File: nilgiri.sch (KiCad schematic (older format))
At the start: 32 parts, among them SW1 SW_PUSH, SW10 SW_PUSH, SW11 SW_PUSH, SW12 SW_PUSH, SW13 SW_PUSH, SW2 SW_PUSH, SW3 SW_PUSH, SW4 SW_PUSH, SW5 SW_PUSH, SW6 SW_PUSH, SW7 SW_PUSH, SW8 SW_PUSH, SW9 SW_PUSH, U1 ProMicro

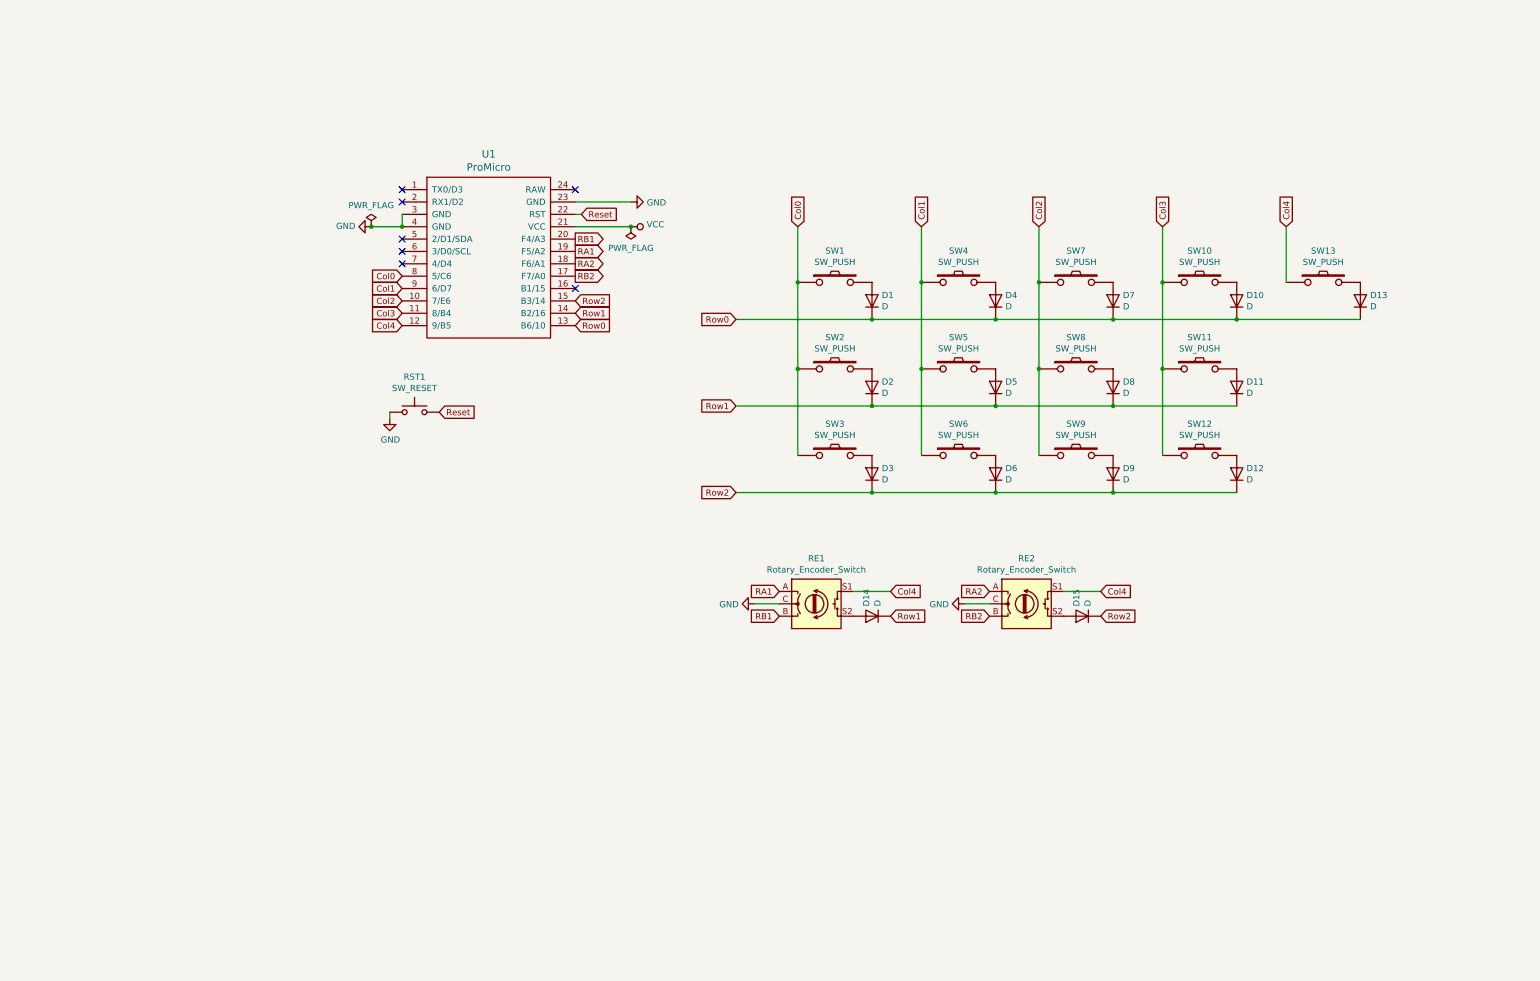
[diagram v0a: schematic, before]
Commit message: merged onboard type / added footprints
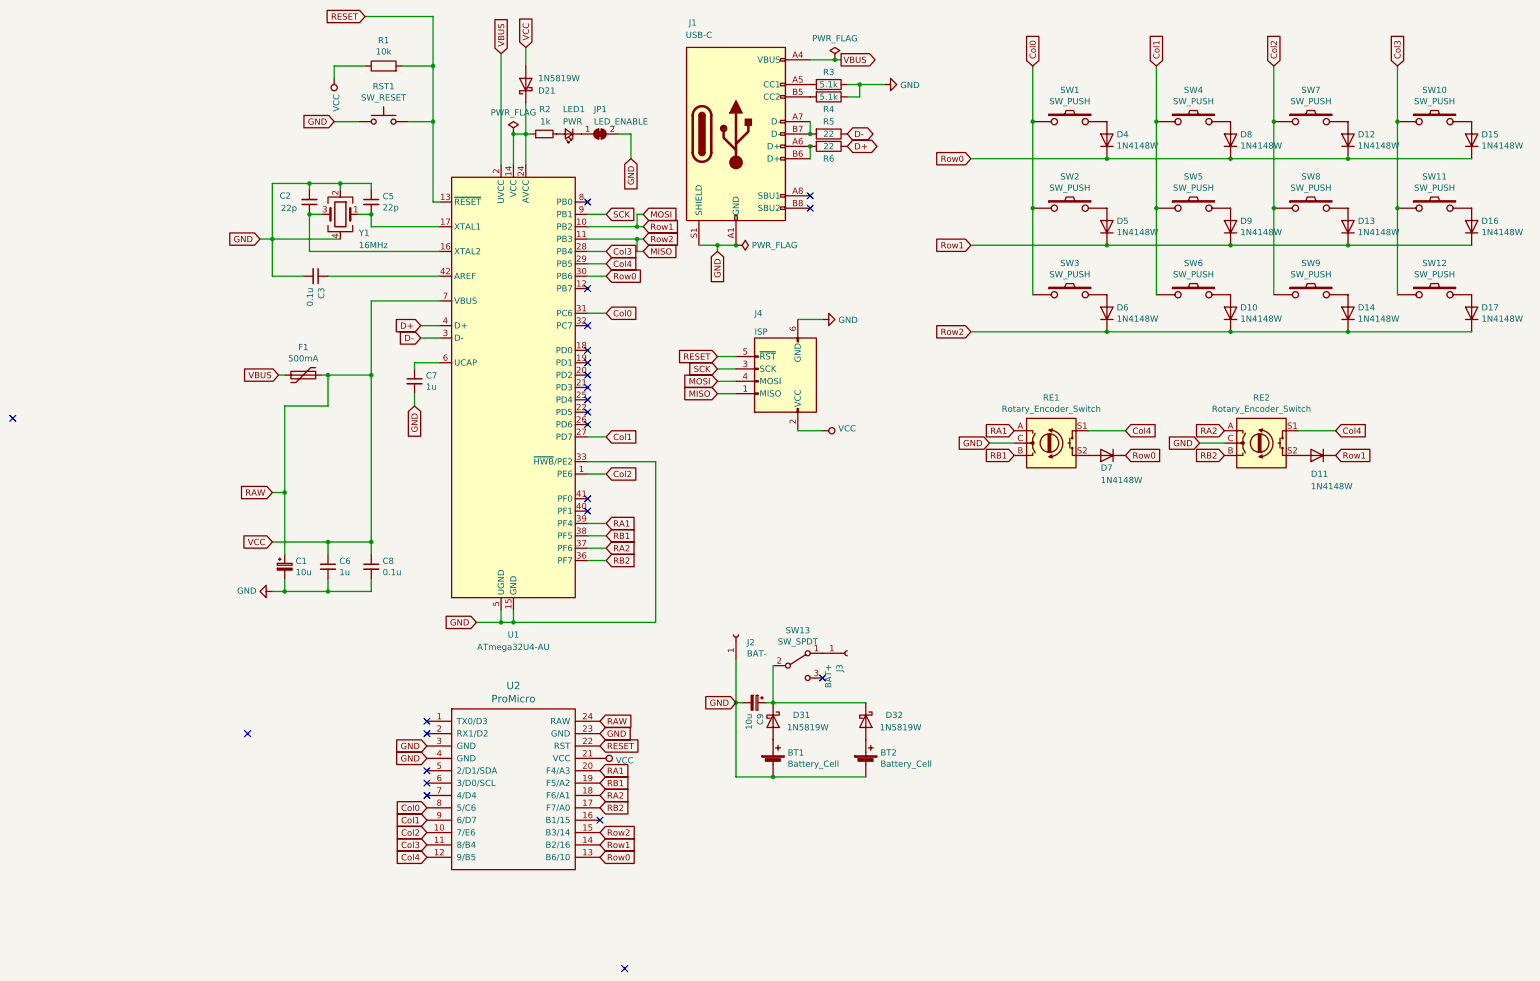
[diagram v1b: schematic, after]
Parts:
- removed D13: D, Keebio:D_SOD123F, symbol Device:D
- removed SW13: SW_PUSH, kbd:CherryMX-Hotswap-v2, symbol kbd:SW_PUSH
- removed U1: ProMicro, kbd:ProMicro_v3, symbol kbd:ProMicro
- added BT1, BT2: Battery_Cell, nilgiri:HU1632, symbol Device:Battery_Cell
- added C1, C9: 10u, Capacitor_Tantalum_SMD:CP_EIA-3216-10_Kemet-I_Pad1.58x1.35mm_HandSolder, symbol Device:CP_Small
- added C2, C5: 22p, Capacitor_SMD:C_0603_1608Metric_Pad1.05x0.95mm_HandSolder, symbol Device:C_Small
- added C3, C8: 0.1u, Capacitor_SMD:C_0603_1608Metric_Pad1.05x0.95mm_HandSolder, symbol Device:C_Small
- added C6, C7: 1u, Capacitor_SMD:C_0603_1608Metric_Pad1.05x0.95mm_HandSolder, symbol Device:C_Small
- added D21, D31, D32: 1N5819W, Keebio:D_SOD123F, symbol Device:D_Schottky
- added F1: 500mA, Fuse:Fuse_1206_3216Metric_Pad1.42x1.75mm_HandSolder, symbol Device:Polyfuse
- added J1: USB-C, Connector_USB:USB_C_Receptacle_Palconn_UTC16-G, symbol Connector:USB_C_Receptacle_USB2.0
- added J2: BAT-, Connector_PinHeader_2.54mm:PinHeader_1x01_P2.54mm_Vertical, symbol Connector:Conn_01x01_Female
- added J3: BAT+, Connector_PinHeader_2.54mm:PinHeader_1x01_P2.54mm_Vertical, symbol Connector:Conn_01x01_Female
- added J4: ISP, Connector_PinHeader_2.54mm:PinHeader_2x03_P2.54mm_Vertical, symbol Connector:AVR-ISP-6
- added JP1: LED_ENABLE, Jumper:SolderJumper-2_P1.3mm_Open_RoundedPad1.0x1.5mm, symbol Jumper:SolderJumper_2_Bridged
- added LED1: PWR, LED_SMD:LED_0603_1608Metric_Pad1.05x0.95mm_HandSolder, symbol Device:LED_Small
- added R1: 10k, Resistor_SMD:R_0603_1608Metric_Pad1.05x0.95mm_HandSolder, symbol Device:R
- added R2: 1k, Resistor_SMD:R_0603_1608Metric_Pad1.05x0.95mm_HandSolder, symbol Device:R_Small
- added R3, R4: 5.1k, Resistor_SMD:R_0603_1608Metric_Pad1.05x0.95mm_HandSolder, symbol Device:R
- added R5, R6: 22, Resistor_SMD:R_0603_1608Metric_Pad1.05x0.95mm_HandSolder, symbol Device:R
- added SW13: SW_SPDT, Button_Switch_SMD:SW_SPDT_PCM12, symbol Switch:SW_SPDT
- added U1: ATmega32U4-AU, Keebio:ATMEGA32U4-AU, symbol MCU_Microchip_ATmega:ATmega32U4-AU
- added U2: ProMicro, kbd:ProMicro_v3, symbol kbd:ProMicro
- added Y1: 16MHz, Crystal:Crystal_SMD_3225-4Pin_3.2x2.5mm, symbol Device:Crystal_GND24
- D10: renamed from D6; value D -> 1N4148W; footprint Keebio:D_SOD123F -> nilgiri:D3_TH_SMD
- D11: renamed from D15; value D -> 1N4148W; footprint Keebio:D_SOD123F -> nilgiri:D3_TH_SMD
- D12: renamed from D7; value D -> 1N4148W; footprint Keebio:D_SOD123F -> nilgiri:D3_TH_SMD
- D13: renamed from D8; value D -> 1N4148W; footprint Keebio:D_SOD123F -> nilgiri:D3_TH_SMD
- D14: renamed from D9; value D -> 1N4148W; footprint Keebio:D_SOD123F -> nilgiri:D3_TH_SMD
- D15: renamed from D10; value D -> 1N4148W; footprint Keebio:D_SOD123F -> nilgiri:D3_TH_SMD
- D16: renamed from D11; value D -> 1N4148W; footprint Keebio:D_SOD123F -> nilgiri:D3_TH_SMD
- D17: renamed from D12; value D -> 1N4148W; footprint Keebio:D_SOD123F -> nilgiri:D3_TH_SMD
- D4: renamed from D1; value D -> 1N4148W; footprint Keebio:D_SOD123F -> nilgiri:D3_TH_SMD
- D5: renamed from D2; value D -> 1N4148W; footprint Keebio:D_SOD123F -> nilgiri:D3_TH_SMD
- D6: renamed from D3; value D -> 1N4148W; footprint Keebio:D_SOD123F -> nilgiri:D3_TH_SMD
- D7: renamed from D14; value D -> 1N4148W; footprint Keebio:D_SOD123F -> nilgiri:D3_TH_SMD
- D8: renamed from D4; value D -> 1N4148W; footprint Keebio:D_SOD123F -> nilgiri:D3_TH_SMD
- D9: renamed from D5; value D -> 1N4148W; footprint Keebio:D_SOD123F -> nilgiri:D3_TH_SMD
- SW1, SW10, SW11, SW12, SW2, SW3, SW4, SW5, SW6, SW7, SW8, SW9: footprint kbd:CherryMX-Hotswap-v2 -> nilgiri:CherryMX_Choc_Hotswap
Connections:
- net Col0: now also U1.31 (PC6), U2.8 (5/C6)
- net Col1: now also U1.27 (PD7), U2.9 (6/D7)
- net Col2: now also U1.1 (PE6), U2.10 (7/E6)
- net Col3: now also U1.28 (PB4), U2.11 (8/B4)
- net Col4: now also U1.29 (PB5), U2.12 (9/B5)
- net GND: now also BT1.2 (-), BT2.2 (-), C1.2, C2.2, C3.2, C5.1, C6.2, C7.2, C8.2, C9.2, J1.A1 (GND), J1.A12 (GND), J1.B1 (GND), J1.B12 (GND), J1.S1 (SHIELD), J2.1 (Pin_1), J4.6 (GND), JP1.2 (B), R3.1, R4.1, U1.15 (GND), U1.23 (GND), U1.33 (~HWB~/PE2), U1.35 (GND), U1.43 (GND), U1.5 (UGND), U2.23 (GND), U2.3 (GND), U2.4 (GND), Y1.2, Y1.4
- net RA1: now also U1.39 (PF4), U2.20 (F4/A3)
- net RA2: now also U1.37 (PF6), U2.18 (F6/A1)
- net RB1: now also U1.38 (PF5), U2.19 (F5/A2)
- net RB2: now also U1.36 (PF7), U2.17 (F7/A0)
- net Row0: now also D7.1 (K), U1.30 (PB6), U2.13 (B6/10)
- net VCC: now also C1.1, C6.1, C8.1, D21.2 (A), F1.1, J4.2 (VCC), R1.1, U1.7 (VBUS), U2.21 (VCC), U2.24 (RAW)
- net Reset renamed RESET
- net RESET: now also J4.5 (~RST), R1.2, U1.13 (~RESET), U2.22 (RST)
- net Row1 renamed MOSI
- net MOSI: now also D11.1 (K), J4.4 (MOSI), U1.10 (PB2), U2.14 (B2/16); no longer D7.1 (K)
- net Row2 renamed MISO
- net MISO: now also J4.1 (MISO), U1.11 (PB3), U2.15 (B3/14); no longer D11.1 (K)
- new net: D21.1 (K), R2.1, U1.14 (VCC), U1.24 (AVCC), U1.34 (VCC), U1.44 (AVCC)
- new net: C2.1, U1.16 (XTAL2), Y1.3
- new net: C5.2, U1.17 (XTAL1), Y1.1
- new net: C3.1, U1.42 (AREF)
- new net: C7.1, U1.6 (UCAP)
- new net: J1.A6 (D+), J1.B6 (D+), R6.2
- new net: J1.A7 (D-), J1.B7 (D-), R5.2
- new net: JP1.1 (A), LED1.1 (K)
- new net: LED1.2 (A), R2.2
- new net: J1.A5 (CC1), R3.2
- new net: J1.B5 (CC2), R4.2
- new net: BT1.1 (+), D31.2 (A)
- new net: BT2.1 (+), D32.2 (A)
- new net: C9.1, D31.1 (K), D32.1 (K), SW13.2 (B)
- new net: J3.1 (Pin_1), SW13.1 (A)
- new net D+: R6.1, U1.4 (D+)
- new net D-: R5.1, U1.3 (D-)
- new net SCK: J4.3 (SCK), U1.9 (PB1)
- new net VBUS: F1.2, J1.A4 (VBUS), J1.A9 (VBUS), J1.B4 (VBUS), J1.B9 (VBUS), U1.2 (UVCC)
- no-connect marks 7 -> 24
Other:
- moved on the sheet: D10, D11, D12, D13, D14, D15, D16, D17, D4, D5, D6, D7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

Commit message: combined Onboard type and Pro Micro type
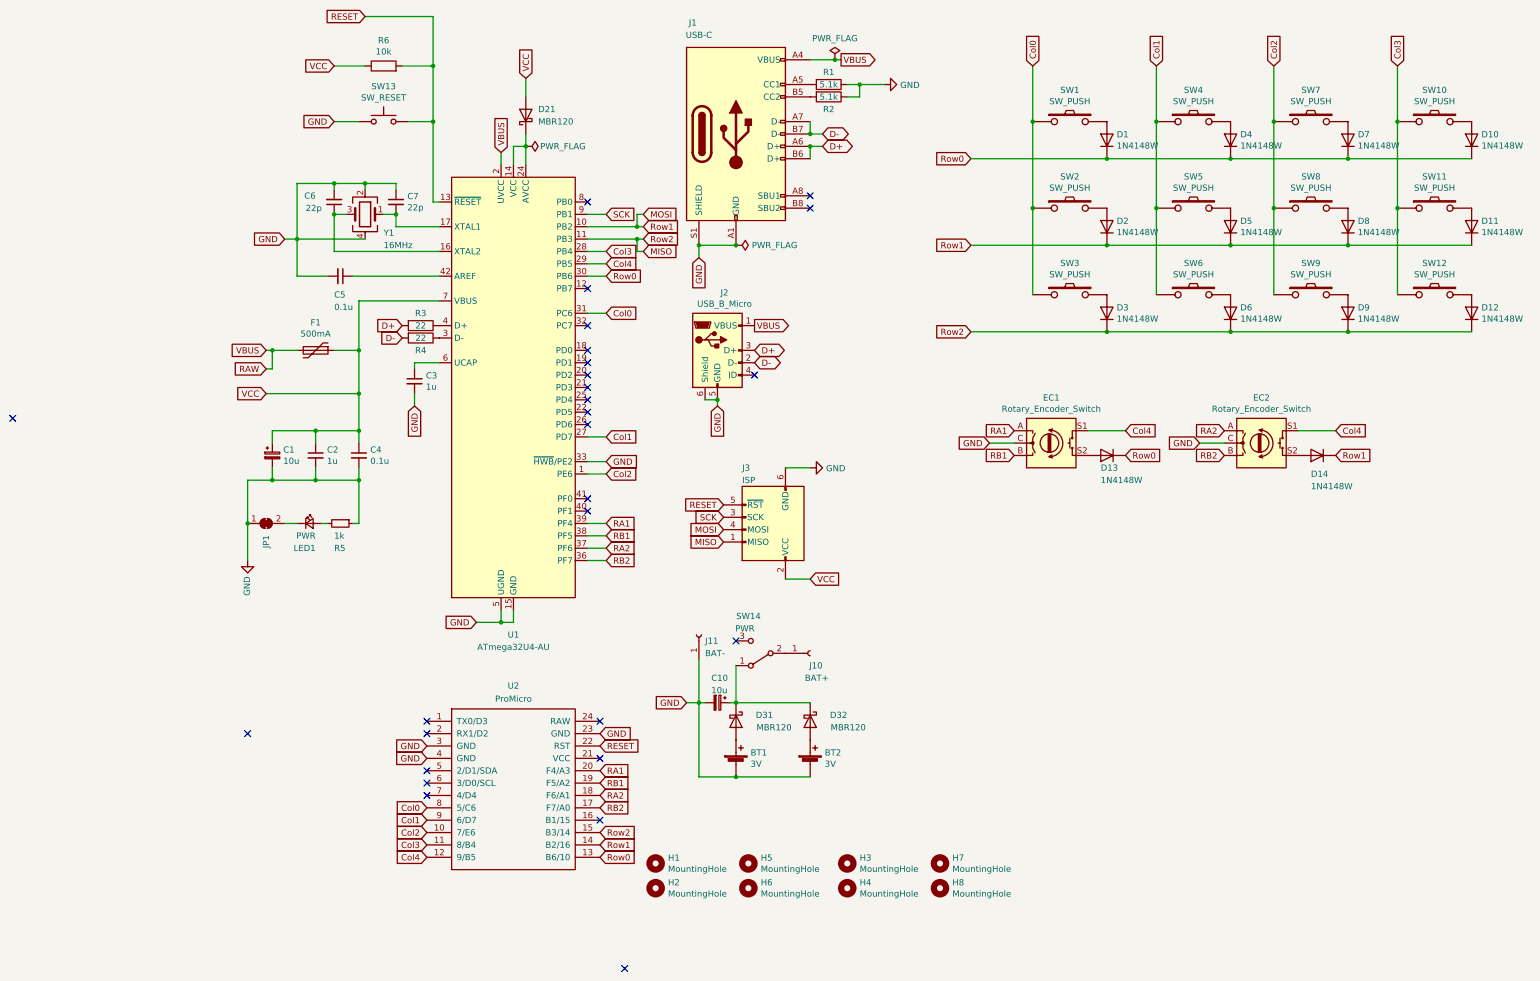
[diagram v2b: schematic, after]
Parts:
- added H1, H2, H3, H4, H5, H6, H7, H8: MountingHole, nilgiri:M2_spacer, symbol Mechanical:MountingHole
- added J2: USB_B_Micro, Connector_USB:USB_Micro-B_Wuerth_629105150521, symbol Connector:USB_B_Micro
- BT1, BT2: value Battery_Cell -> 3V
- D21, D31, D32: value 1N5819W -> MBR120
- SW1, SW10, SW11, SW12, SW2, SW3, SW4, SW5, SW6, SW7, SW8, SW9: footprint nilgiri:CherryMX_Choc_Hotswap -> kbd:CherryMX_Choc_1u
- SW14: renamed from SW13; value SW_SPDT -> PWR
- renumbered C9 to C10, C6 to C2, C7 to C3, C8 to C4, C3 to C5, C2 to C6, C5 to C7, D4 to D1, D15 to D10, D16 to D11, D17 to D12, D7 to D13, D11 to D14, D5 to D2, D6 to D3, D8 to D4, D9 to D5, D10 to D6, D12 to D7, D13 to D8, D14 to D9, RE1 to EC1, RE2 to EC2, J3 to J10, J2 to J11, J4 to J3, R3 to R1, R4 to R2, R5 to R3, R6 to R4, R2 to R5, R1 to R6, RST1 to SW13
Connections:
- net D+: now also J1.A6 (D+), J1.B6 (D+), R3.2, J2.3 (D+); no longer R4.1, U1.4 (D+)
- net D-: now also J1.A7 (D-), J1.B7 (D-), R4.2, J2.2 (D-); no longer R3.1, U1.3 (D-)
- net GND: now also JP1.1 (A), R5.1, J2.5 (GND), J2.6 (Shield); no longer JP1.2 (B)
- net VCC: no longer U2.21 (VCC), U2.24 (RAW)
- net at D21.1 (K), U1.14 (VCC), U1.24 (AVCC)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: no longer R5.1
- net at LED1.1 (K): now also JP1.2 (B); no longer JP1.1 (A)
- net at C10.1, D31.1 (K), D32.1 (K): now also SW14.1 (A); no longer SW14.2 (B)
- net at J10.1 (Pin_1): now also SW14.2 (B); no longer SW14.1 (A)
- net VBUS renamed RAW
- net RAW: now also J2.1 (VBUS)
- new net: R4.1, U1.3 (D-)
- new net: R3.1, U1.4 (D+)
- no-connect marks 24 -> 27
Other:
- moved on the sheet: BT1, BT2, C1, C10, C2, C4, C5, C6, C7, D21, D31, D32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

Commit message: 全体調整
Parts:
- added H99: LOGO, nilgiri:nil_logo, symbol Mechanical:MountingHole
- EC1, EC2: value Rotary_Encoder_Switch -> EC11E18244A5
- H1, H2, H3, H4: footprint nilgiri:M2_spacer -> nilgiri:M2_vis
- J10, J11: footprint Connector_PinHeader_2.54mm:PinHeader_1x01_P2.54mm_Vertical -> nilgiri:Hole 0.8mm
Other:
- moved on the sheet: H1, H2, H3, H4, H5, H6, H7, H8
